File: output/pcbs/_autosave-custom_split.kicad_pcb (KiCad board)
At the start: 2 copper layers, 135.1 x 84 mm, 39 parts

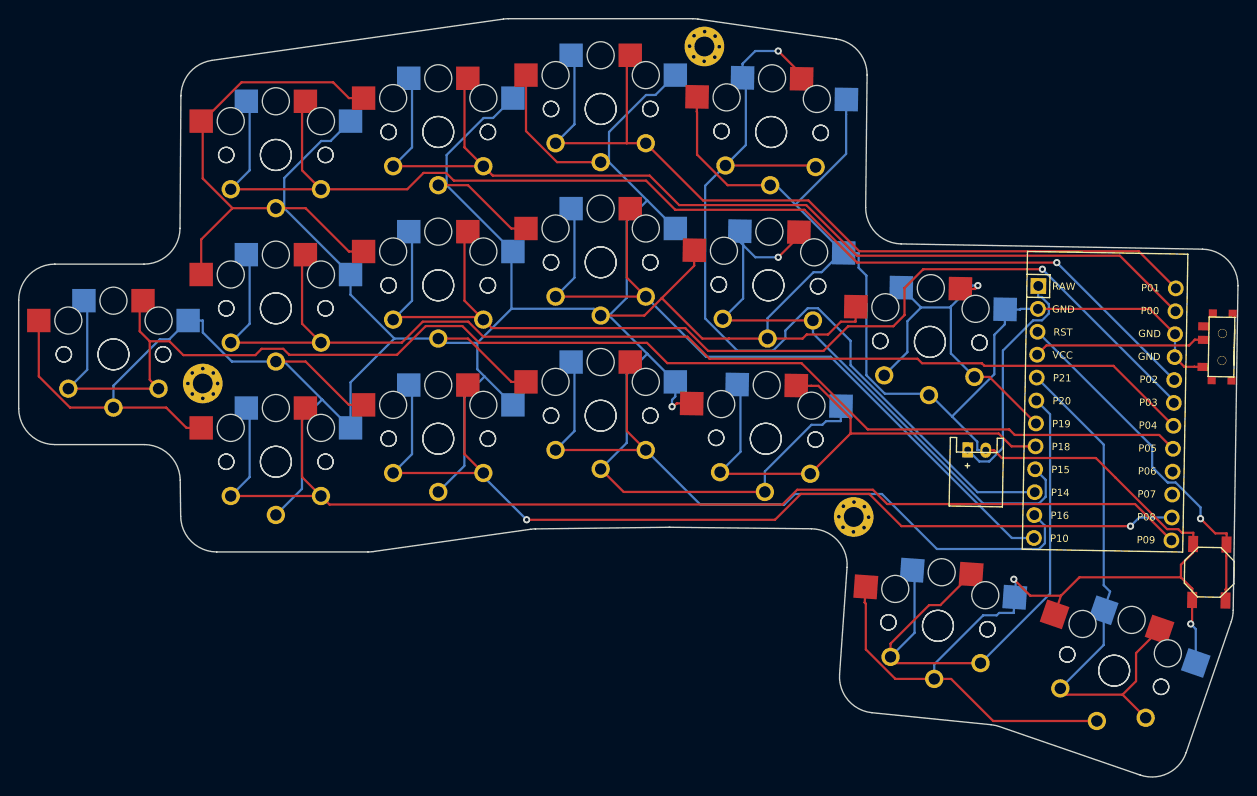
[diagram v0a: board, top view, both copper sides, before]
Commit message: switched the footprint to one that didn't clip pads; no more errors in kicad
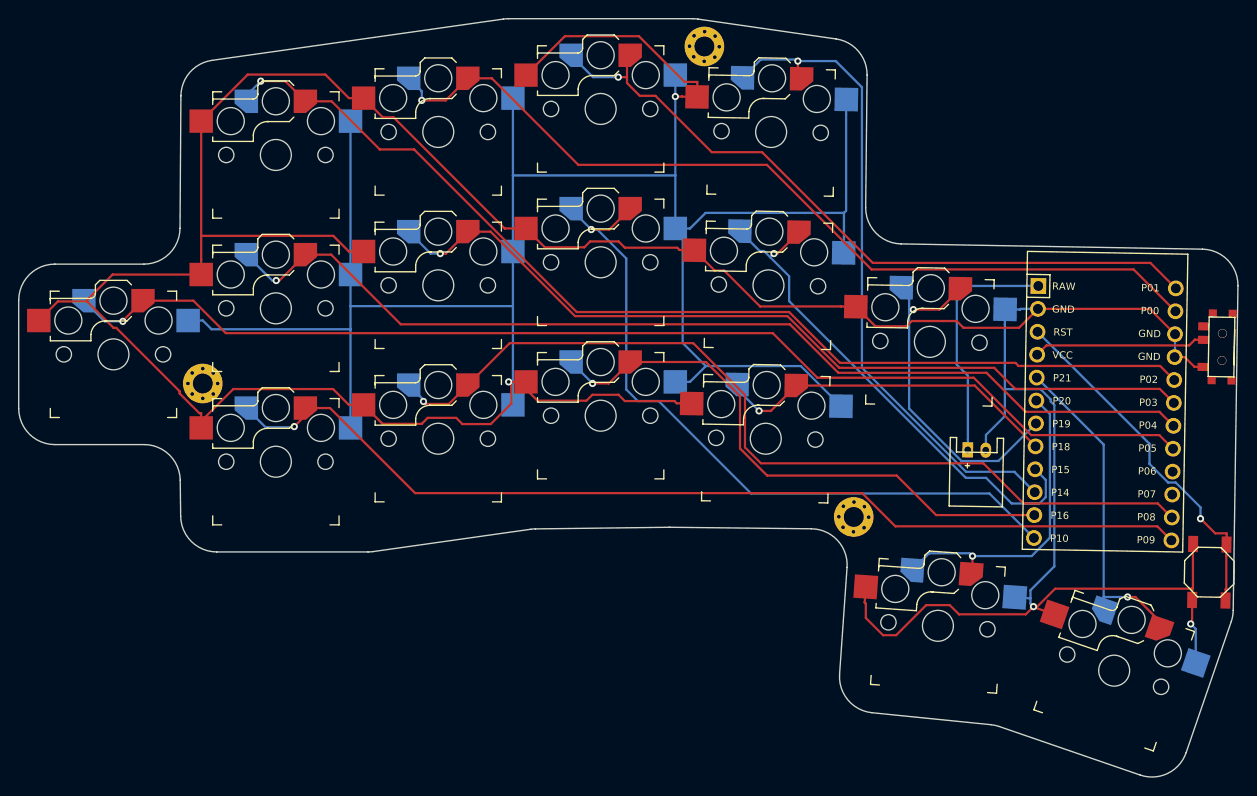
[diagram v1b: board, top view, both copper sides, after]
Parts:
- removed S17, S18, S19, S20, S21, S22, S23, S24, S25, S26, S27, S28, S29, S30, S31, S32: , PG1350
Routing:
- net GND: track 701.9 -> 622.0 mm, vias 3 -> 4
- net P20: track 67.6 -> 34.9 mm, vias 0 -> 1
- net P3: track 121.3 -> 94.7 mm
- net P14: track 99.5 -> 73.4 mm
- net P5: track 153.1 -> 129.4 mm, vias 0 -> 1
- net P21: track 59.6 -> 37.1 mm, vias 0 -> 1
- net P16: track 85.2 -> 63.7 mm, vias 0 -> 1
- net P18: track 57.5 -> 38.5 mm, vias 0 -> 1
- net P4: track 131.8 -> 113.0 mm, vias 0 -> 1
- net P2: track 136.4 -> 117.9 mm
- net P9: track 129.2 -> 110.9 mm, vias 0 -> 1
- net P0: track 114.9 -> 98.3 mm, vias 0 -> 1
- net P1: track 96.1 -> 80.7 mm, vias 0 -> 1
- net P8: track 113.3 -> 99.8 mm, vias 2 -> 1
- net P15: track 69.6 -> 56.2 mm
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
